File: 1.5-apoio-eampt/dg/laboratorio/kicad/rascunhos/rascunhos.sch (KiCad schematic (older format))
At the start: 17 parts

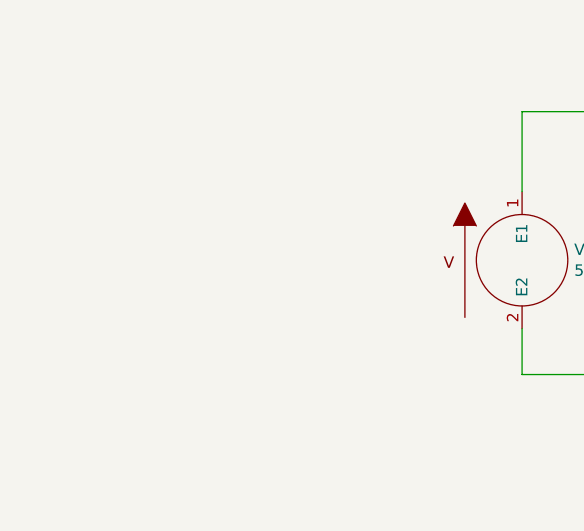
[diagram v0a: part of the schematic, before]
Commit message: Reestruturação do diretório do Dado Digital. Início do projeto do Dado Digital Simplificado.
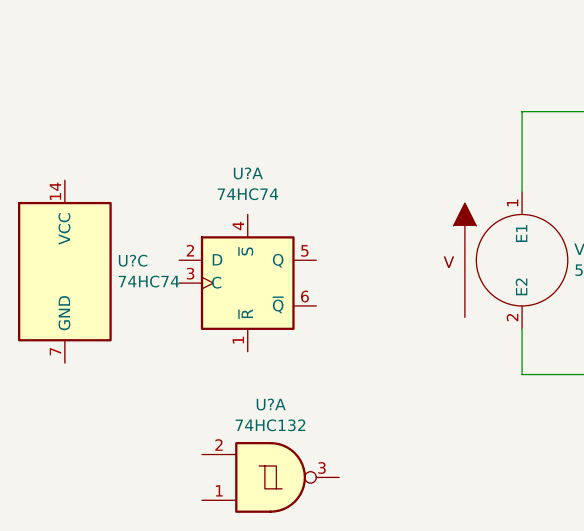
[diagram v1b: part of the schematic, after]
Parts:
- added U? (x2): 74HC74, symbol 74xx:74HC74
- added U?: 74HC132, symbol 74xx:74LS132
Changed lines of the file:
@@
 Wire Wire Line
 	8000 2150 8150 2150
+$Comp
+L 74xx:74HC74 U?
+U 1 1 5EE2F309
+P 2250 4050
+F 0 "U?" H 2250 4528 50  0000 C CNN
+F 1 "74HC74" H 2250 4437 50  0000 C CNN
+F 2 "" H 2250 4050 50  0001 C CNN
+F 3 "74xx/74hc_hct74.pdf" H 2250 4050 50  0001 C CNN
+	1    2250 4050
+	1    0    0    -1
+$EndComp
+$Comp
+L 74xx:74HC74 U?
+U 3 1 5EE2F856
+P 1450 4000
+F 0 "U?" H 1680 4046 50  0000 L CNN
+F 1 "74HC74" H 1680 3955 50  0000 L CNN
+F 2 "" H 1450 4000 50  0001 C CNN
+F 3 "74xx/74hc_hct74.pdf" H 1450 4000 50  0001 C CNN
+	3    1450 4000
+	1    0    0    -1
+$EndComp
+$Comp
+L 74xx:74LS132 U?
+U 1 1 5EE2FA36
+P 2350 4900
+F 0 "U?" H 2350 4583 50  0000 C CNN
+F 1 "74HC132" H 2350 4674 50  0000 C CNN
+F 2 "" H 2350 4900 50  0001 C CNN
+F 3 "http://www.ti.com/lit/gpn/sn74LS132" H 2350 4900 50  0001 C CNN
+	1    2350 4900
+	1    0    0    1
+$EndComp
 $EndSCHEMATC
